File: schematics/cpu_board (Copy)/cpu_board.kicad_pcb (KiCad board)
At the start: 2 copper layers, 150.3 x 100.3 mm, 68 parts, among them J600 Euro96pin, J601 clock, J602 clock1, J602_1 clock_dtack, J603 Conn_02x08_Counter_Clockwise, J604 systemTickFreq, J605 Conn_01x32, Q7 2N3904, Q8 2N3904, SW1 Reset, U600 68000D, U600rst1 ICM7555xB, U601 74LS393, U602 74HC164, U603 74HC14, U604 ATmega8-16P, U605 74LS20, U606 74HC4078, U607 74LS139

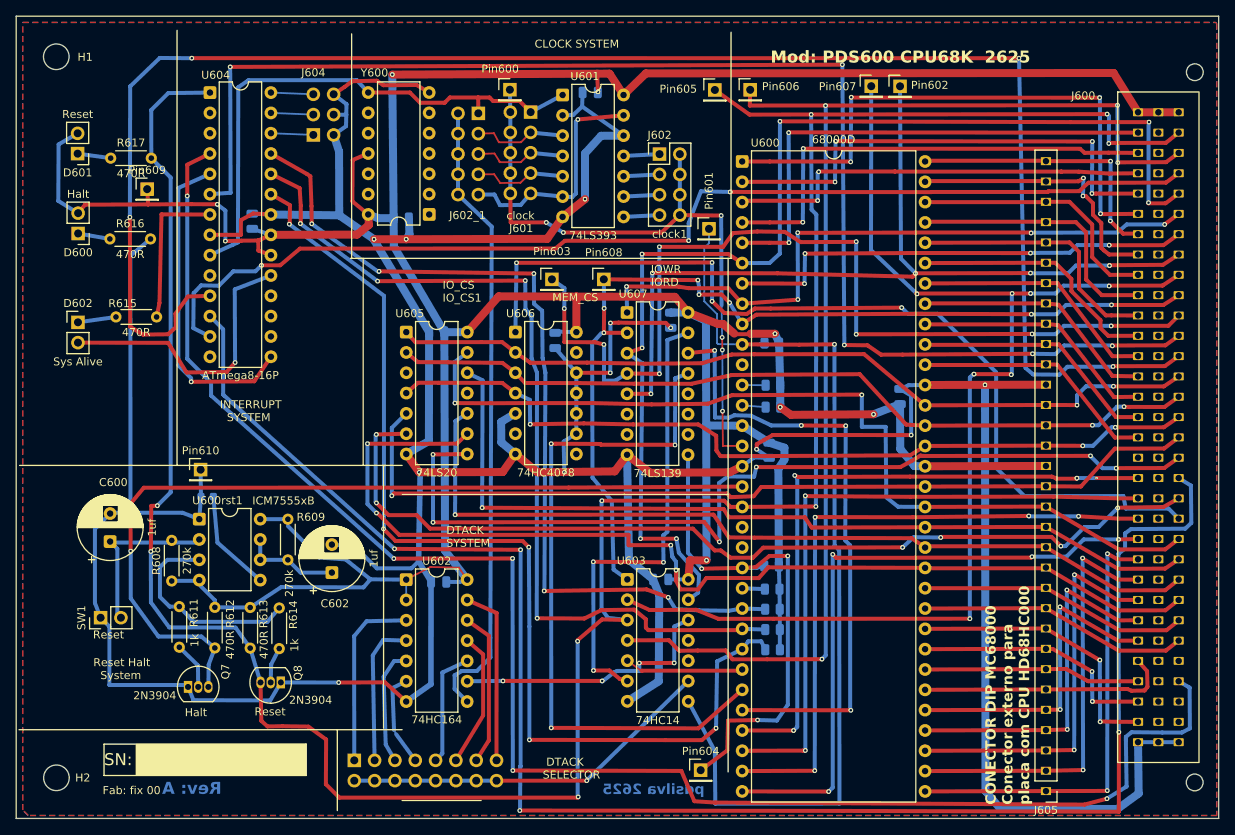
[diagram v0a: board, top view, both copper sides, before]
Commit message: PDS600 100% routed
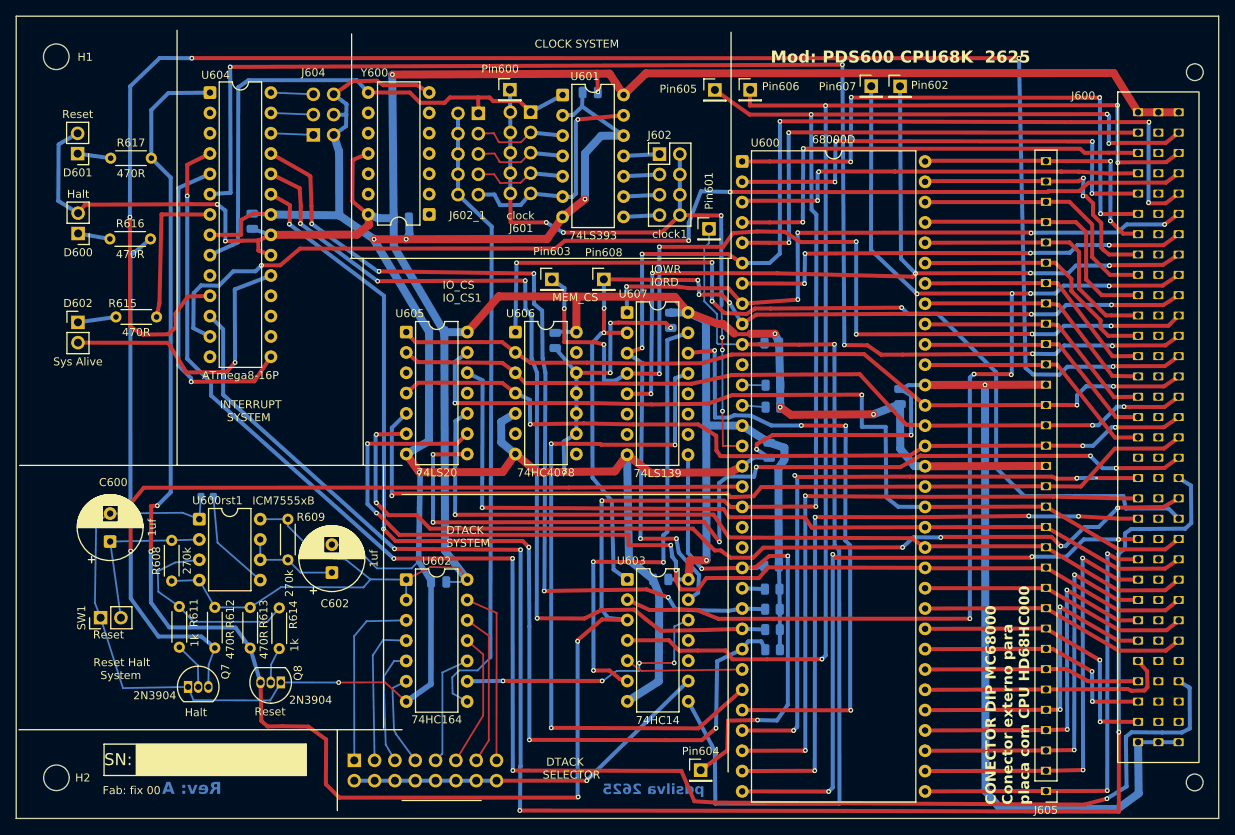
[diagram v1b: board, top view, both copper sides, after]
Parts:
- removed Pin609: Vcc, Connector_PinHeader_2.54mm:PinHeader_1x01_P2.54mm_Vertical
- removed Pin610: gnd, Connector_PinHeader_2.54mm:PinHeader_1x01_P2.54mm_Vertical
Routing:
- net GND: track 523.1 -> 518.5 mm
- net +5V: track 490.4 -> 488.2 mm
- net Net-(SW1-Pin_2): track 21.7 -> 20.8 mm
- net //IPL1: track 112.1 -> 111.4 mm
- net Net-(U600rst1-Q): track 26.1 -> 25.4 mm
- net Net-(J602_1-Pin_10): track 79.1 -> 79.7 mm
- removed copper zone on B.Cu, net GND
- removed copper zone on F.Cu, net GND
